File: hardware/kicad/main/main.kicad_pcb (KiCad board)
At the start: 2 copper layers, 116 x 137.5 mm, 59 parts, among them J1 USB_C_Receptacle_USB2.0, J10 ENC_LEFT, J11 ENC_RIGHT, J12 UART0, J2 SERVO_L, J3 SERVO_R, J4 Conn_01x02_Pin, J8 Conn_02x10_Odd_Even, Q1 2N7002K, SW1 SW_SPST, SW2 SW_SPST, SW3 SW_SPST, SW4 SW_SPST, U2 AP1117-33, U5 IP5306, U6 ESP32-S3-WROOM-1

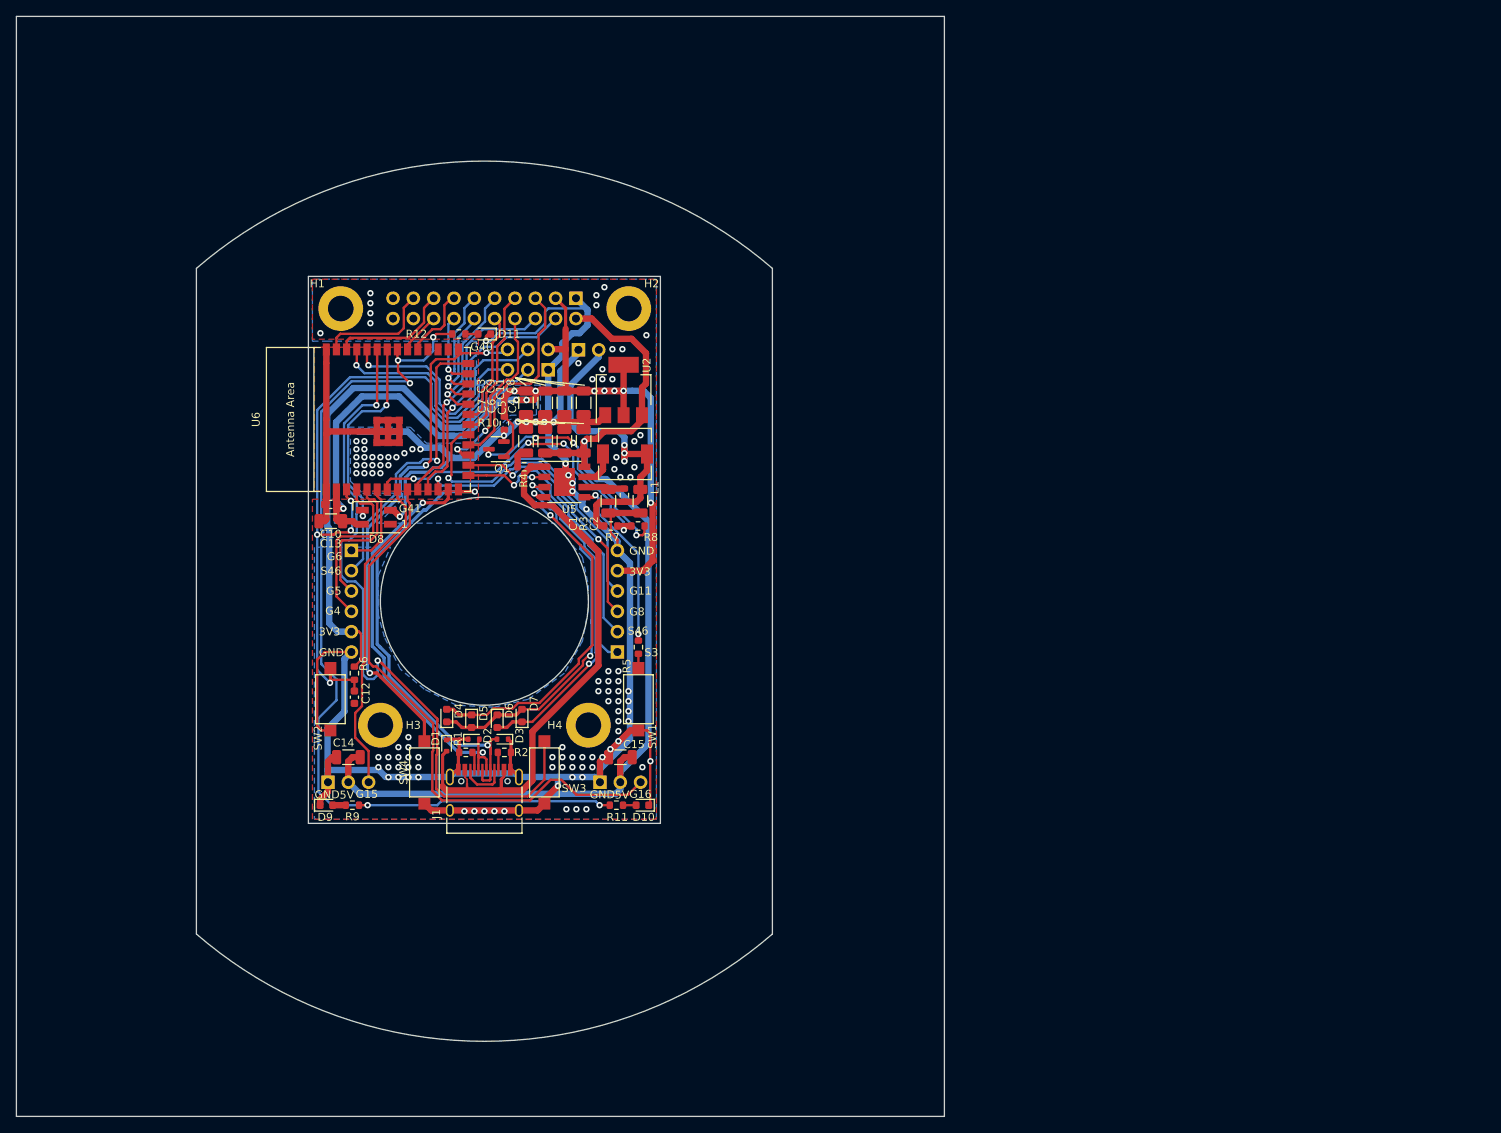
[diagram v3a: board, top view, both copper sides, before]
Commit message: changed buttons to basic ones, fixed inductor footprint, added JLCPCB part numbers to each mounted component for assembly
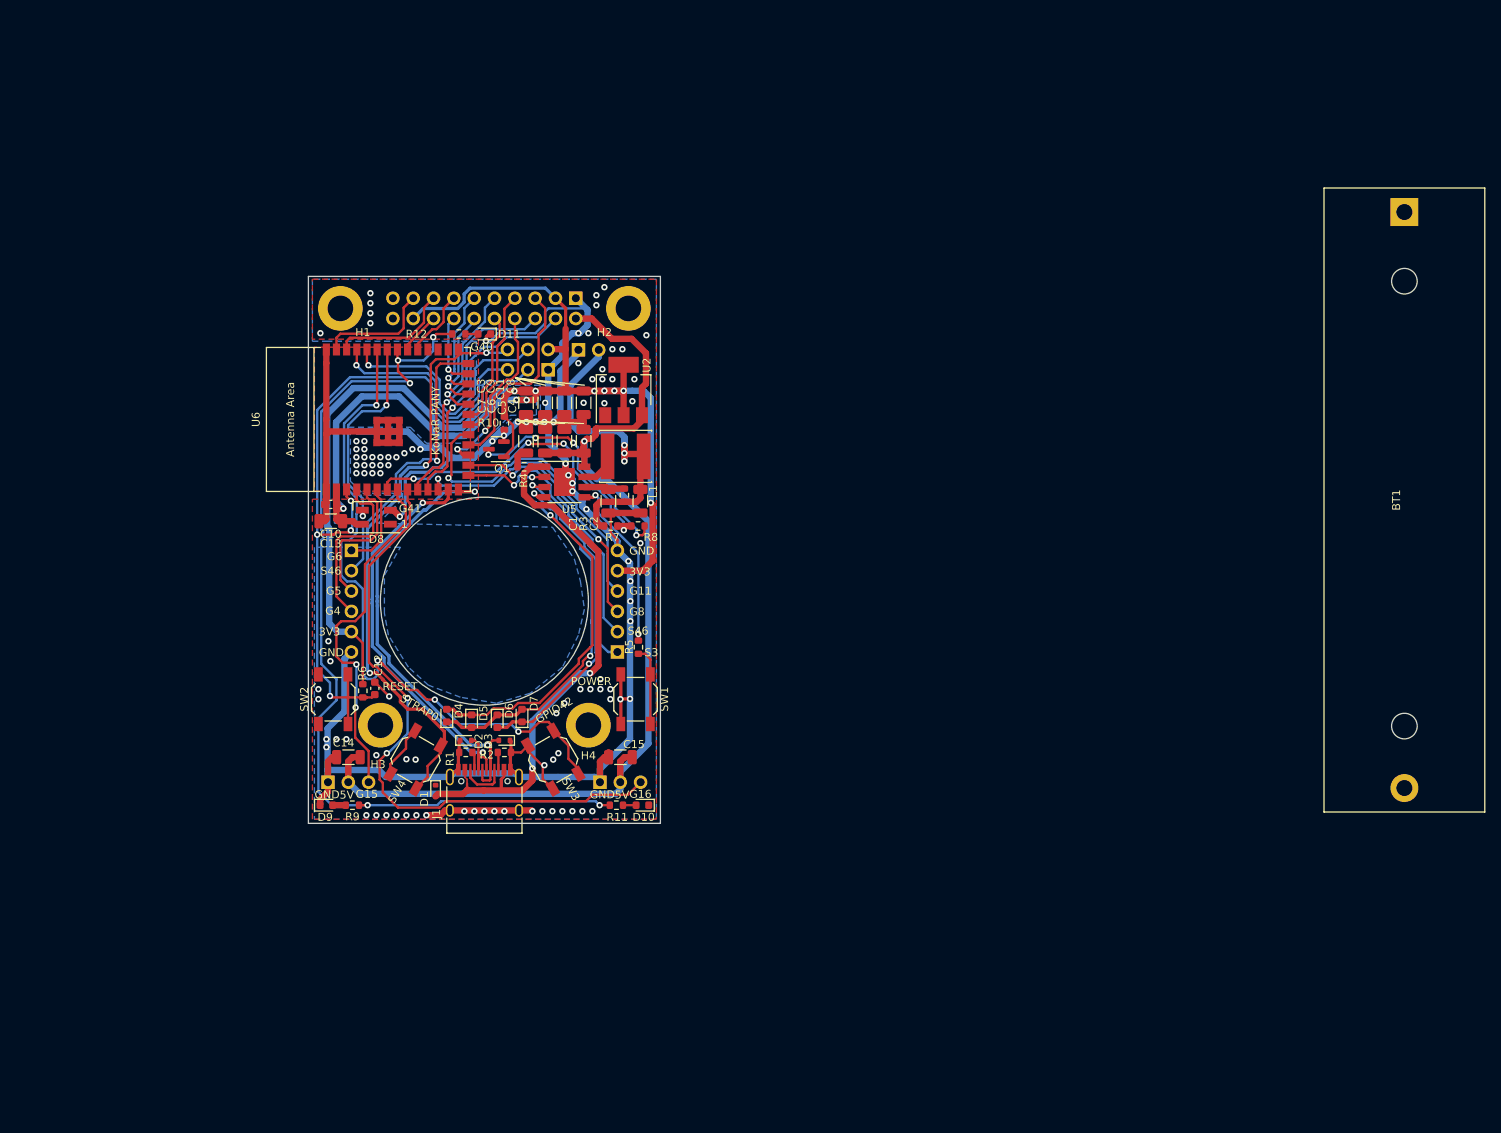
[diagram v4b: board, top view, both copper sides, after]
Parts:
- added BT1: 18650, Battery:BatteryHolder_MPD_BH-18650-PC2, F.Cu at (215.0, 51.4)
- J4: value Conn_01x02_Pin -> BAT
- L1: value L -> 1u; footprint Inductor_SMD:L_6.3x6.3_H3 -> Inductor_SMD:L_Changjiang_FNR6020S
- R11, R12, R9: value 1k -> 150
- SW1, SW2, SW3, SW4: footprint Button_Switch_SMD:SW_SPST_CK_RS282G05A3 -> Button_Switch_SMD:SW_SPST_SKQG_WithStem
- moved D1 5.81 mm to (93.9, 123.7)
- moved C12 2.78 mm to (86.3, 110.9), turned to 90 degrees
- moved R6 2.44 mm to (84.8, 111.2)
- moved SW3 1.94 mm to (108.6, 119.8), turned to 120 degrees
- moved SW4 1.94 mm to (91.4, 119.8), turned to 60 degrees
- moved D2 1.01 mm to (97.7, 117.4)
- moved SW1 0.35 mm to (118.9, 112.2)
- moved SW2 0.35 mm to (81.1, 112.2)
- moved L1 0.31 mm to (117.7, 81.9)
- moved D3 0.27 mm to (102.5, 117.4)
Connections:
- J8 pad 18: unconnected-(J8-Pin_18-Pad18) -> +3.3V
- J8 pad 20: unconnected-(J8-Pin_20-Pad20) -> GND
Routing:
- net +3.3V: track 206.8 -> 228.7 mm
- net GND: track 350.4 -> 333.7 mm, vias 120 -> 108
- net /STRAP0: track 66.1 -> 75.6 mm
- net Net-(SW1-A): track 1.77 -> 9.88 mm
- net /~{RST}: track 87.0 -> 94.7 mm
- net /GPIO16: track 72.5 -> 78.4 mm, vias 0 -> 2
- net /GPIO42: track 90.4 -> 84.8 mm, vias 2 -> 4
- net /GPIO15: track 40.3 -> 44.3 mm, vias 0 -> 2
- net Net-(J4-Pin_2): track 41.0 -> 44.0 mm
- net +5VD: track 72.7 -> 69.7 mm, vias 0 -> 2
- net /USB_D-: track 52.7 -> 54.2 mm
- net /USB_D+: track 58.5 -> 59.6 mm
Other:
- board size 116 x 137.5 mm -> 44 x 68.4 mm
- board text added: "1523 REV A HaD Prize Crunch"
- board text added: "GPIO42"
- board text added: "KoNaR PANY"
- board text added: "POWER"
- board text added: "RESET"
- board text added: "STRAP0"
- board text added: "kabot.io"

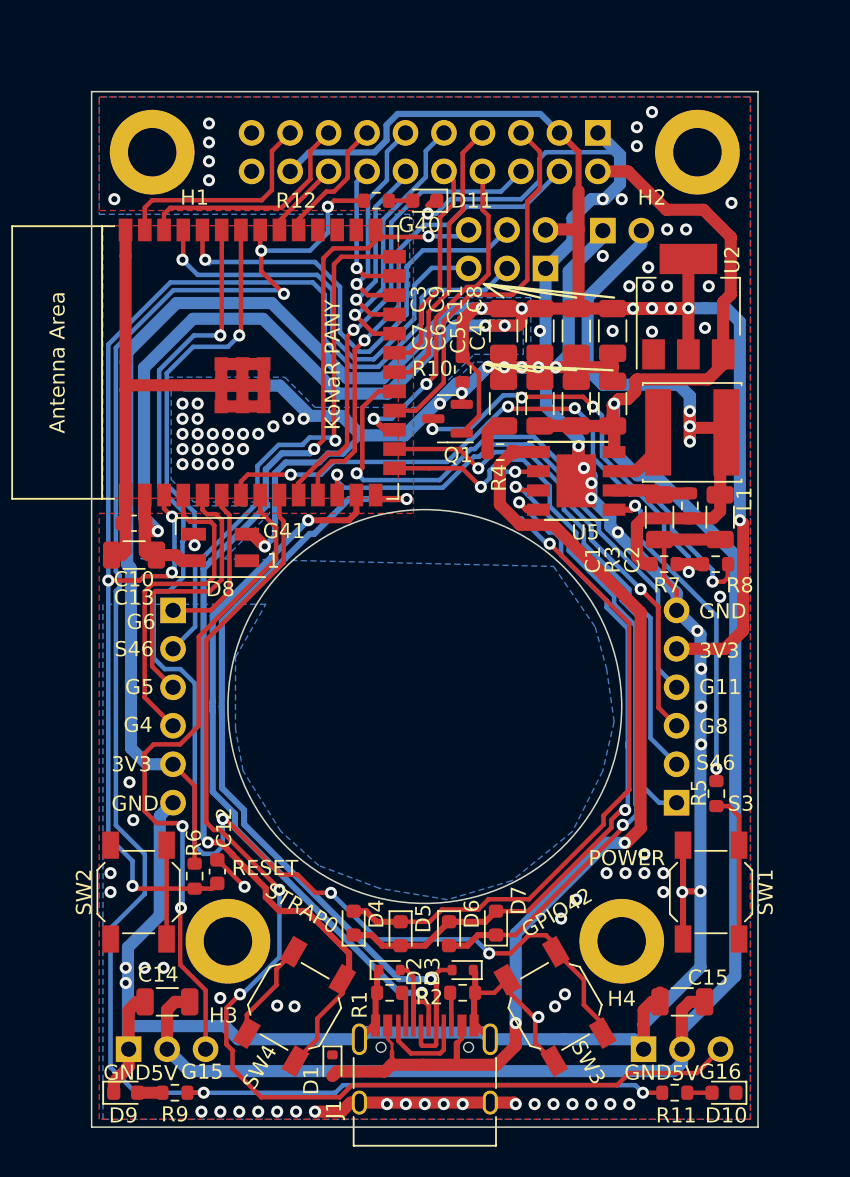
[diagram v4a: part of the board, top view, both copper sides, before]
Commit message: minor dimensions adjustments
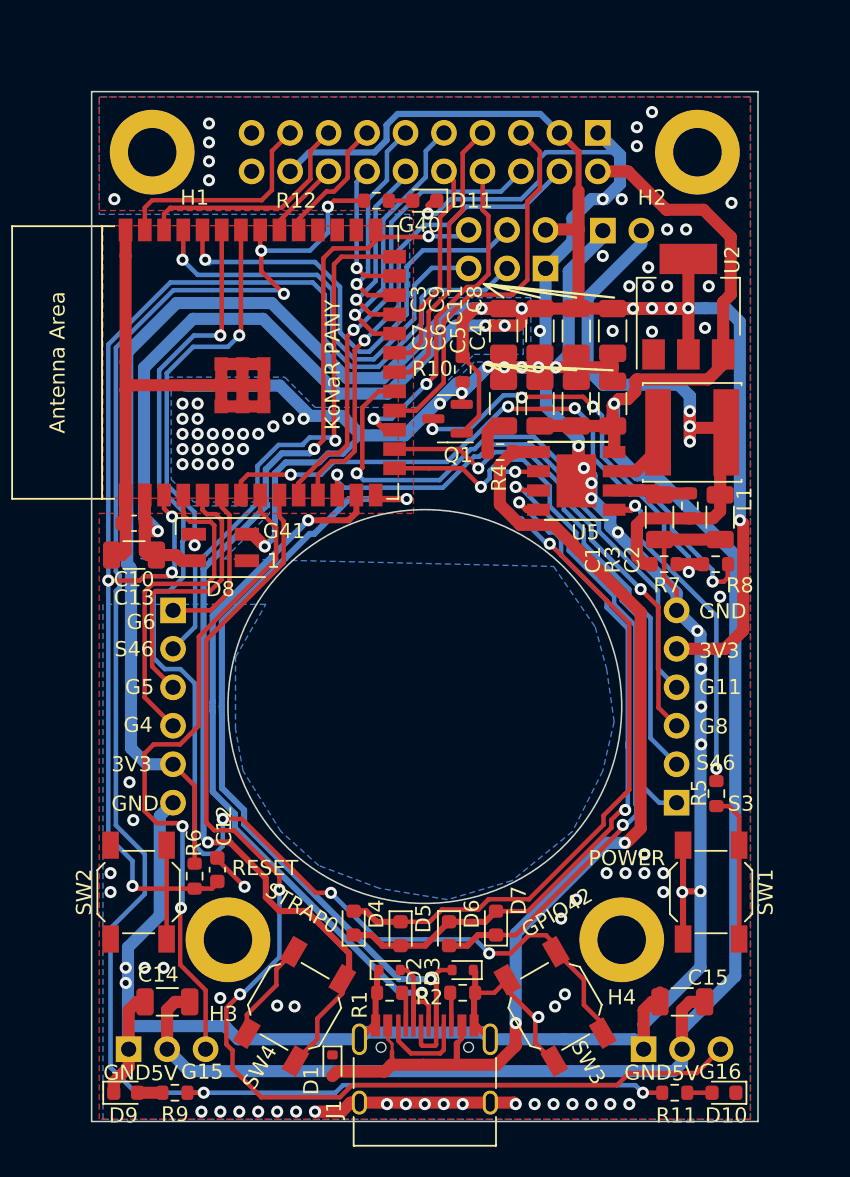
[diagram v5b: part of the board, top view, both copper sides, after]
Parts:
- moved C12 0.12 mm to (86.3, 110.8)
- moved H3 0.10 mm to (87.0, 115.4)
- moved H4 0.10 mm to (113.0, 115.4)
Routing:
- net /GPIO16: track 78.4 -> 78.9 mm
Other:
- board size 44 x 68.4 mm -> 44 x 68 mm

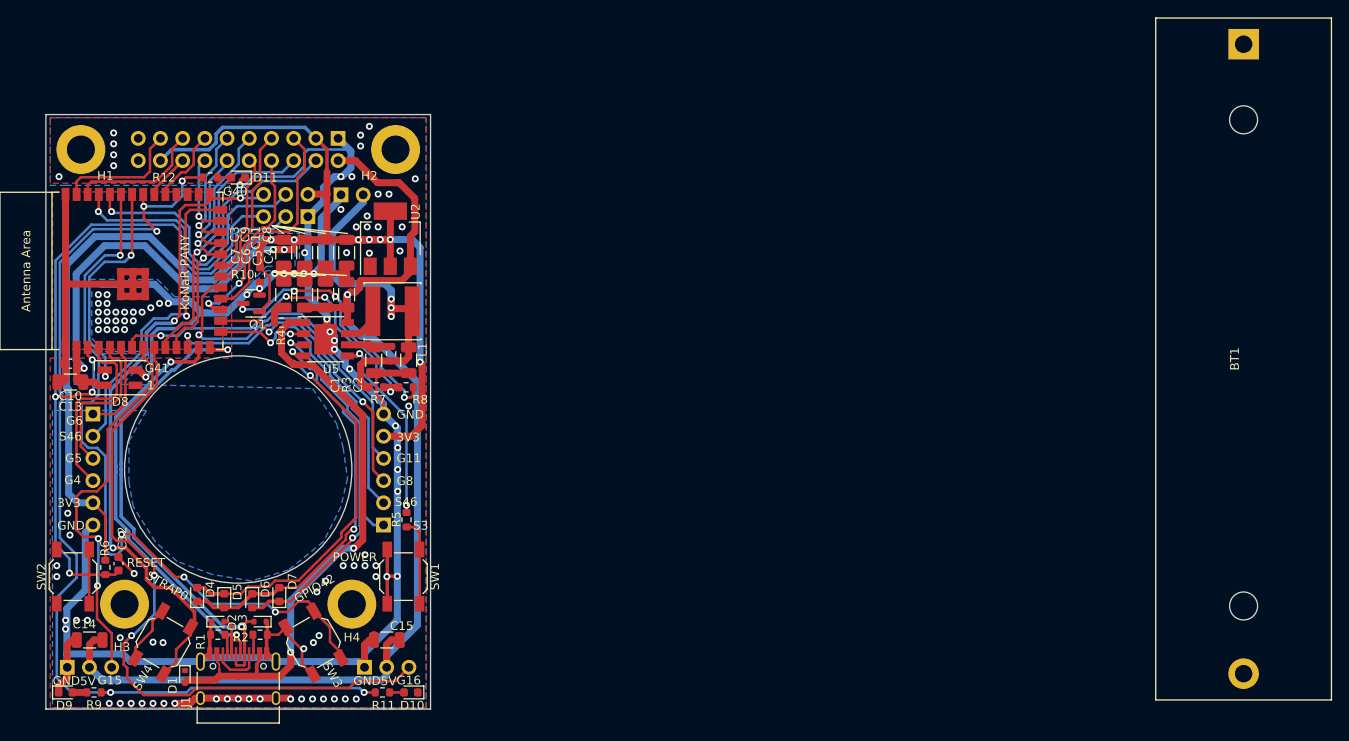
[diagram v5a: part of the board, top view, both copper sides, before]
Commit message: removed addressable led as it is not really available, fixed inductor footprint, added production files
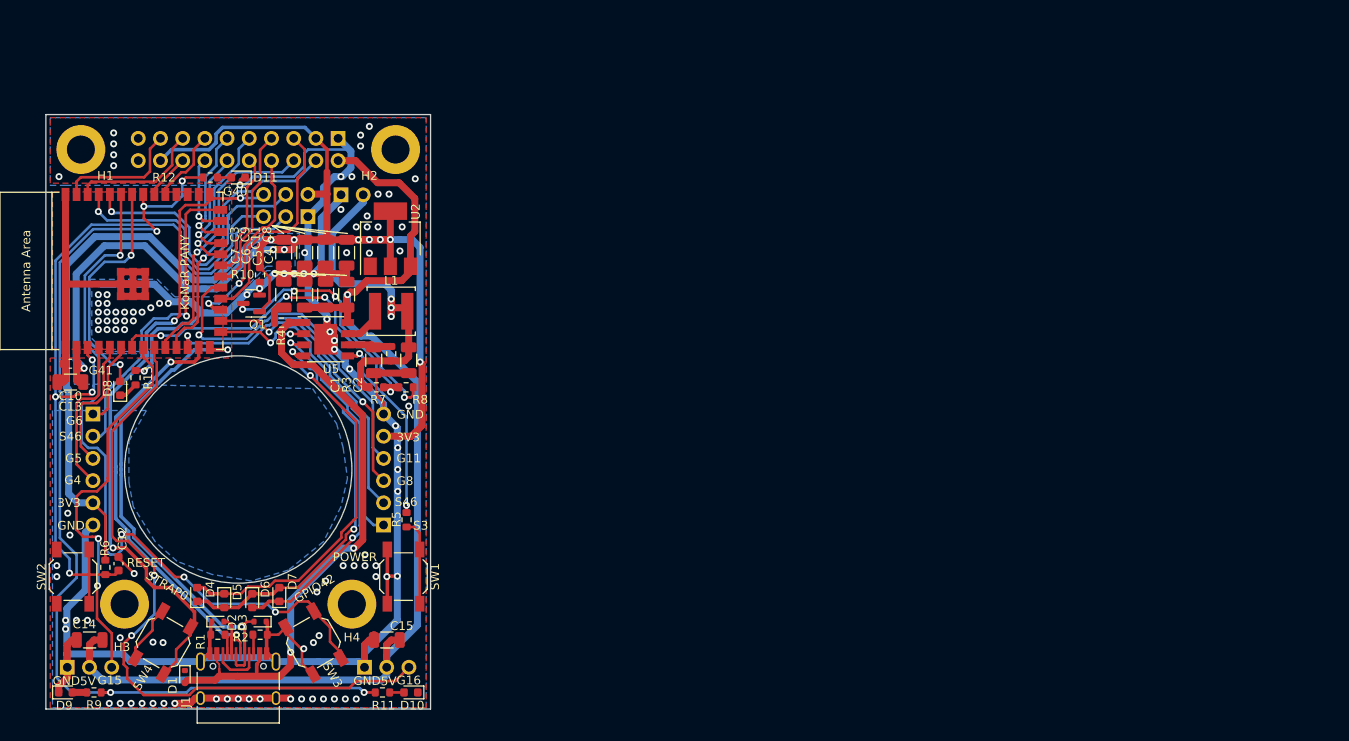
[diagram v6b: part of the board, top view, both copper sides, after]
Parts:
- removed BT1: 18650, Battery:BatteryHolder_MPD_BH-18650-PC2
- added R13: 5k1, Resistor_SMD:R_0603_1608Metric, F.Cu at (88.2, 89.5)
- D8: value SK6812MINI -> R; footprint LED_SMD:LED_SK6812MINI_PLCC4_3.5x3.5mm_P1.75mm -> LED_SMD:LED_0603_1608Metric
- L1: footprint Inductor_SMD:L_Changjiang_FNR6020S -> Inductor_SMD:L_Changjiang_FNR5045S
- moved D8 1.21 mm to (86.5, 90.7), turned to 90 degrees
- moved L1 0.15 mm to (117.5, 81.9)
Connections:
- D8 pad 1: unconnected-(D8-DOUT-Pad1) -> Net-(D8-K)
- D8 pad 2: GND -> /GPIO41
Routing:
- net /GPIO4: track 21.6 -> 18.0 mm
- net +3.3V: track 228.7 -> 226.0 mm
- net /GPIO5: track 18.1 -> 15.6 mm
- net Net-(D8-K): track 0.00 -> 2.24 mm
- net Net-(J4-Pin_2): track 44.0 -> 42.7 mm
- net /GPIO6: track 10.8 -> 9.58 mm
- net GND: track 333.7 -> 332.6 mm
- net /GPIO41: track 25.7 -> 26.7 mm
- net /STRAP45: track 36.6 -> 37.1 mm
